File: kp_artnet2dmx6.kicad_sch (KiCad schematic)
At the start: 0 parts

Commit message: add stm32
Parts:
- added C1, C10, C3, C4, C5, C6, C7, C8: 100n, symbol Device:C_Small
- added C2: 10u, symbol Device:C_Small
- added C9: 1u, symbol Device:C_Small
- added FB1, FB2, FB3: 600@100MHz, symbol Device:FerriteBead_Small
- added R1: R_Small, symbol Device:R_Small
- added SW1: SW_SPDT, symbol Switch:SW_SPDT
- added U1: STM32F407VETx, Package_QFP:LQFP-100_14x14mm_P0.5mm, symbol MCU_ST_STM32F4:STM32F407VETx
- added Y1: 16MHz, symbol Device:Crystal_GND24_Small
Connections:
- new net: Y1.2 (G), Y1.4 (G)
- new net: R1.2, SW1.2 (B)
- new net +3.3V: C2.1, C3.1, C4.1, C5.1, C6.1, C7.1, C8.1, FB1.2, SW1.3 (C), U1.100 (VDD), U1.11 (VDD), U1.19 (VDD), U1.28 (VDD), U1.50 (VDD), U1.6 (VBAT), U1.75 (VDD)
- new net +3.3VA: C10.1, C9.1, FB1.1, FB3.2, U1.22 (VDDA)
- new net +3.3VREF: C1.1, FB3.1, U1.21 (VREF+)
- new net GND: C2.2, C3.2, C4.2, C5.2, C6.2, C7.2, C8.2, FB2.2, SW1.1 (A), U1.10 (VSS), U1.27 (VSS), U1.74 (VSS), U1.99 (VSS)
- new net GNDA: C1.2, C10.2, C9.2, FB2.1, U1.20 (VSSA)
- new net STM_BOOT0: R1.1, U1.94 (BOOT0)
- new net STM_HSE_IN: U1.12 (PH0)
- new net STM_HSE_OUT: U1.13 (PH1)
- new net STM_NRST: U1.14 (NRST)
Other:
- note added: "BOOT0: LOW for normal boot HIGH for bootloader"
- note added: "TODO"
- note added: "decoupling caps + vdd/vdda connection"

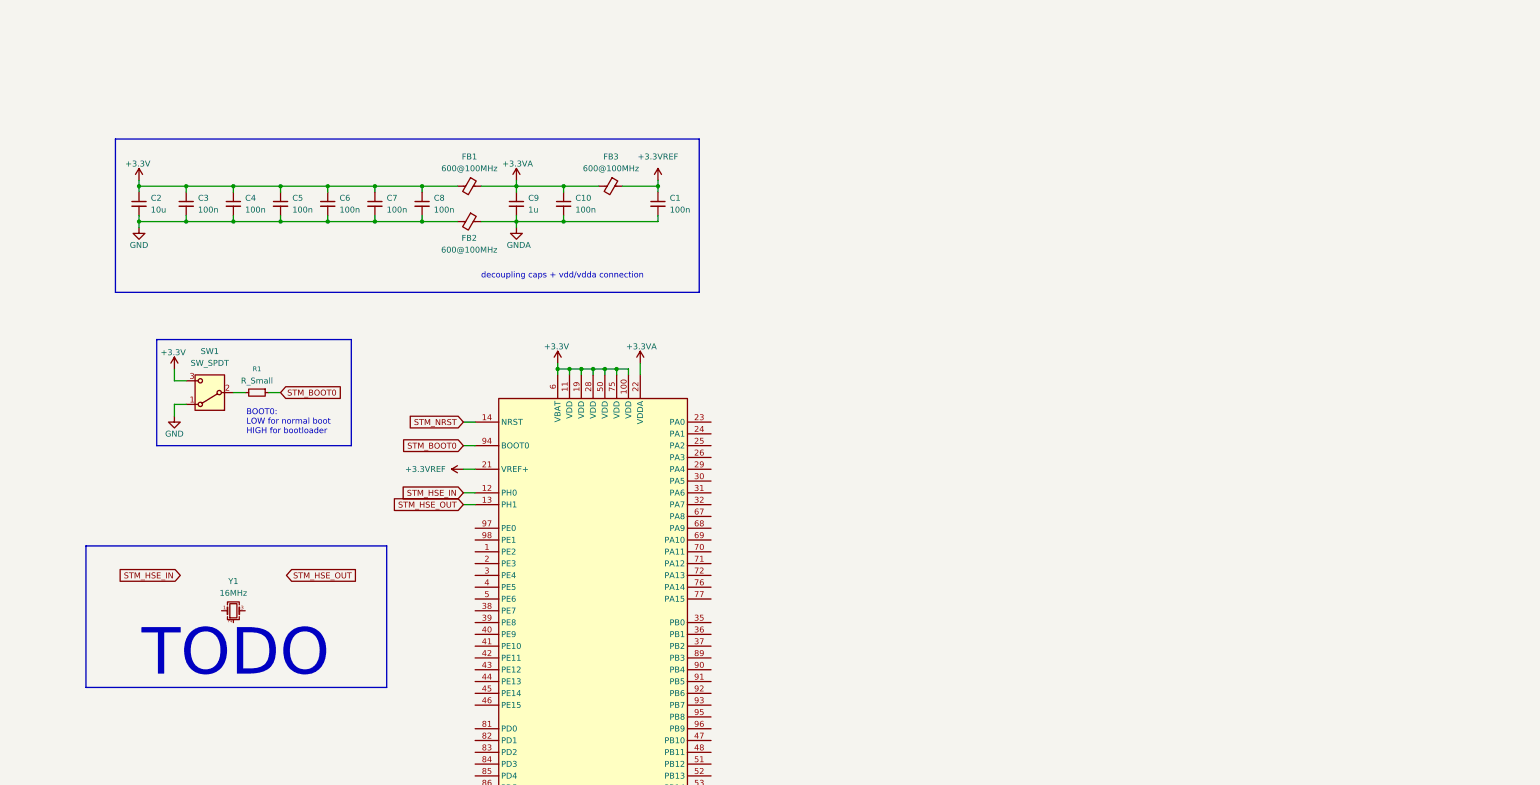
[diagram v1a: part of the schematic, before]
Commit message: sch: add phy, add oscillator
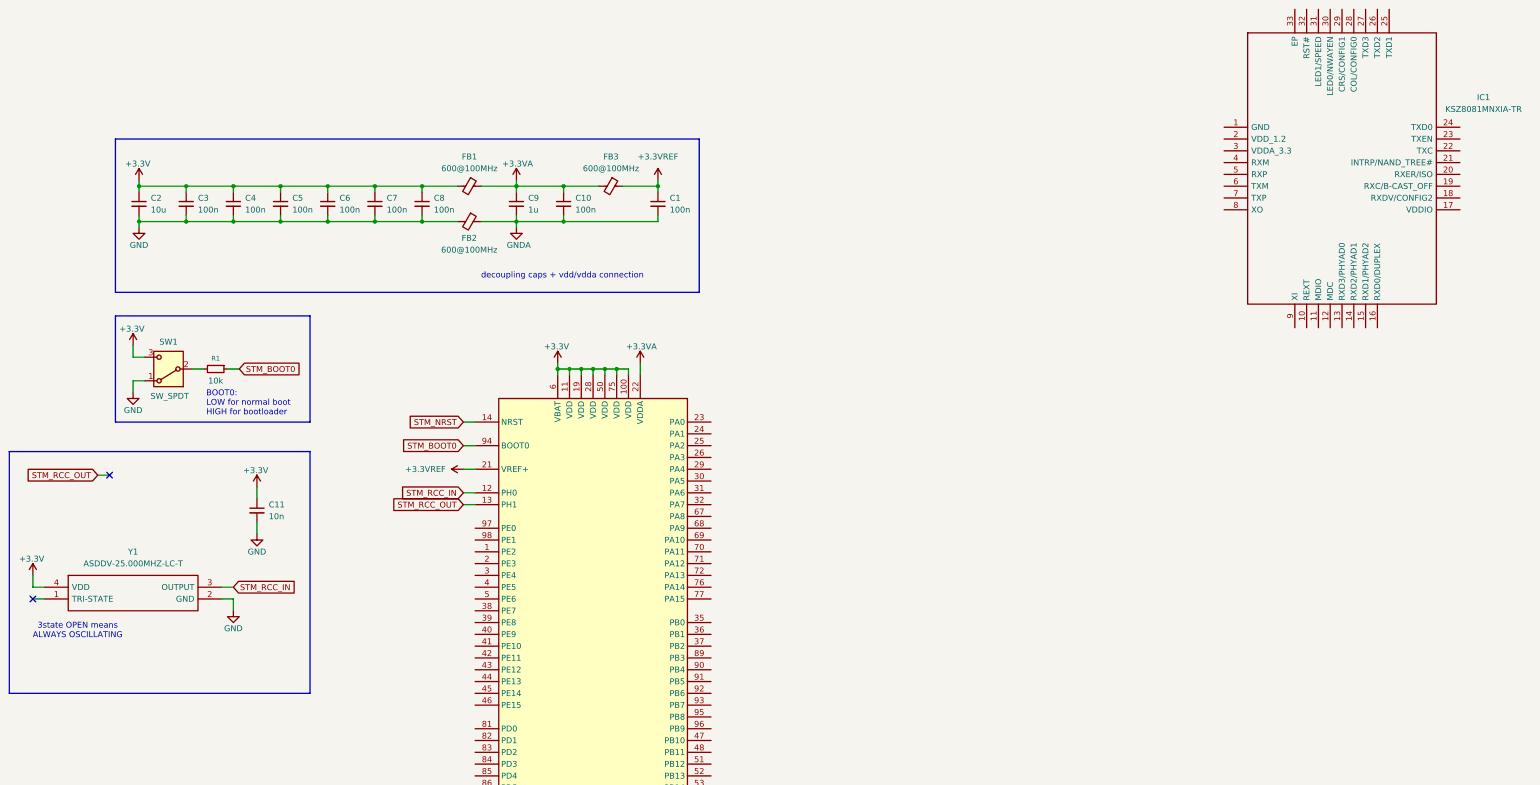
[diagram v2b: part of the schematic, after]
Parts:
- removed Y1: 16MHz, symbol Device:Crystal_GND24_Small
- added C11: 10n, symbol Device:C_Small
- added IC1: KSZ8081MNXIA-TR, QFN50P500X500X100-33N-D, symbol SamacSys:KSZ8081MNXIA-TR
- added Y1: ASDDV-25.000MHZ-LC-T, AbraconASDDV, symbol SamacSys:ASDDV-25.000MHZ-LC-T
- R1: value R_Small -> 10k
- SW1: footprint (none) -> Button_Switch_SMD:SW_SPDT_PCM12
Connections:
- net +3.3V: now also C11.1, Y1.4 (VDD)
- net GND: now also C11.2, Y1.2 (GND)
- net STM_HSE_IN renamed STM_RCC_IN
- net STM_RCC_IN: now also Y1.3 (OUTPUT)
- net STM_HSE_OUT renamed STM_RCC_OUT
- no-connect marks 0 -> 2
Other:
- note added: "3state OPEN means ALWAYS OSCILLATING"
- note removed: "TODO"
- moved on the sheet: R1, SW1

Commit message: add ksz eth controller, todo finish connecting it
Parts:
- added C12: 2.2u, symbol Device:C_Small
- added C13, C17, C19: 100n, symbol Device:C_Small
- added C16, C18: 22u, symbol Device:C_Small
- added FB5: 600@100MHz, symbol Device:FerriteBead_Small
- added J1: RJ45_Amphenol_RJMG1BD3B8K1ANR, Connector_RJ:RJ45_Amphenol_RJMG1BD3B8K1ANR, symbol Connector:RJ45_Amphenol_RJMG1BD3B8K1ANR
- added R2: 1k, symbol Device:R_Small
- added R3: 4.49k, symbol Device:R_Small
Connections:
- net +3.3V: now also IC1.17 (VDDIO), C16.1, C17.1, FB5.2, R2.2
- net GND: now also IC1.1 (GND), C12.2, C13.2, C16.2, C17.2, C18.2, C19.2, R3.1
- net at IC1.10 (REXT): now also R3.2
- net STM_ETH_MDIO: now reaches IC1.11 (MDIO)
- net STM_ETH_MDIO: now also U1.25 (PA2), R2.1
- net STM_ETH_MDC: now reaches IC1.12 (MDC)
- net STM_ETH_MDC: now also U1.16 (PC1)
- net KSZ_VDD_1.2: now reaches IC1.2 (VDD_1.2)
- net KSZ_VDDA_3.3: now reaches IC1.3 (VDDA_3.3)
- net KSZ_VDDA_3.3: now also C18.1, C19.1, FB5.1
- net KSZ_RXM: now reaches IC1.4 (RXM)
- net KSZ_RXM: now also J1.R6 (RD-)
- net KSZ_RXP: now reaches IC1.5 (RXP)
- net KSZ_RXP: now also J1.R3 (RD+)
- net KSZ_TXM: now reaches IC1.6 (TXM)
- net KSZ_TXM: now also J1.R2 (TD-)
- net KSZ_TXP: now reaches IC1.7 (TXP)
- net KSZ_TXP: now also J1.R1 (TD+)
- net STM_RCC_MCO_1: now reaches IC1.9 (XI)
- net STM_RCC_MCO_1: now also U1.67 (PA8)
- net STM_ETH_TXD3: now reaches U1.1 (PE2)
- net STM_ETH_TXD2: now reaches U1.17 (PC2)
- net STM_ETH_CRS: now reaches U1.23 (PA0)
- net STM_ETH_RX_CLK: now reaches U1.24 (PA1)
- net STM_ETH_COL: now reaches U1.26 (PA3)
- net STM_ETH_RX_DV: now reaches U1.32 (PA7)
- net STM_ETH_RXD0: now reaches U1.33 (PC4)
- net STM_ETH_RXD1: now reaches U1.34 (PC5)
- net STM_ETH_RXD2: now reaches U1.35 (PB0)
- net STM_ETH_RXD3: now reaches U1.36 (PB1)
- net STM_ETH_TX_EN: now reaches U1.48 (PB11)
- net STM_ETH_TXD0: now reaches U1.51 (PB12)
- net STM_ETH_TXD1: now reaches U1.52 (PB13)
- new net KSZ_VDD_1.2V: C12.1, C13.1
- no-connect marks 2 -> 3
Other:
- note added: "KSZ8081MNX/RNB POWER PIN DESCRIPTIONS Power Pin Pin Number Description VDD_1.2 2 Decouple with 2.2 μF and 0.1 μF capacitors to ground. VDDA_3.3 3 Connect to board's 3.3V supply through a ferrite bead. Decouple with 22 μF and 0.1 μF capacitors to ground. VDDIO 17 Connect to board's 3.3V supply for 3.3V VDDIO. Decouple with 22 μF and 0.1 μF capacitors to ground."
- moved on the sheet: IC1

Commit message: connect ksz
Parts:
- added C14: 10uF, symbol Device:C_Polarized_Small
- added C15, C20: 100n, symbol Device:C_Small
- added D1: 1N4148, Diode_THT:D_DO-35_SOD27_P7.62mm_Horizontal, symbol Diode:1N4148
- added R10, R12, R13, R15, R16, R4, R9: 1k, symbol Device:R_Small
- added R11, R14, R17, R18, R7, R8: 4.7k, symbol Device:R_Small
- added R5, R6: 220, symbol Device:R_Small
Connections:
- net +3.3V: now also D1.1 (K), R11.1, R14.2, R17.1, R18.1, R5.1, R6.1, R7.1, R8.1
- net GND: now also IC1.33 (EP), J1.R8, J1.SH, C14.2, C15.2, C20.1, R10.1, R12.2, R13.2, R15.1, R16.1, R4.2, R9.1
- net STM_ETH_COL: now also IC1.28 (COL/CONFIG0), R16.2
- net STM_ETH_CRS: now also IC1.29 (CRS/CONFIG1), R15.2
- net STM_ETH_RXD0: now also IC1.16 (RXD0/DUPLEX), R11.2
- net STM_ETH_RXD1: now also IC1.15 (RXD1/PHYAD2), R10.2
- net STM_ETH_RXD2: now also IC1.14 (RXD2/PHYAD1), R9.2
- net STM_ETH_RXD3: now also IC1.13 (RXD3/PHYAD0), R8.2
- net STM_ETH_RX_CLK: now also IC1.19 (RXC/B-CAST_OFF), R12.1
- net STM_ETH_RX_DV: now also IC1.18 (RXDV/CONFIG2), R4.1
- net STM_ETH_TXD0: now also IC1.24 (TXD0)
- net STM_ETH_TXD1: now also IC1.25 (TXD1)
- net STM_ETH_TXD2: now also IC1.26 (TXD2)
- net STM_ETH_TXD3: now also IC1.27 (TXD3)
- net STM_ETH_TX_EN: now also IC1.23 (TXEN)
- net at J1.L1: now also R5.2
- net KSZ_LED0: now reaches J1.L2
- net KSZ_LED0: now also IC1.30 (LED0/NWAYEN), R17.2
- net KSZ_LED1: now reaches J1.L3
- net KSZ_LED1: now also IC1.31 (LED1/SPEED), R18.2
- net at J1.L4: now also R6.2
- net at J1.R4 (TCT): now also C15.1
- net at J1.R5 (RCT): now also C20.2
- net STM_ETH_RXERR_GPIO: now reaches IC1.20 (RXER/ISO)
- net STM_ETH_RXERR_GPIO: now also U1.40 (PE9), R13.1
- net STM_ETH_INT_GPIO: now reaches IC1.21 (INTRP/NAND_TREE#)
- net STM_ETH_INT_GPIO: now also U1.39 (PE8), R14.1
- net STM_ETH_TX_CLK: now reaches IC1.22 (TXC)
- net STM_ETH_TX_CLK: now also U1.18 (PC3)
- net KSZ_RST: now reaches IC1.32 (RST#)
- net KSZ_RST: now also U1.38 (PE7), C14.1, D1.2 (A), R7.2
- net STM_RCC_MCO_2: now reaches U1.66 (PC9)
- net STM_RCC_MCO_2: now also IC1.9 (XI)
- net KSZ_RXM renamed KSZ_RX-
- net KSZ_RXP renamed KSZ_RX+
- net KSZ_TXM renamed KSZ_TX-
- net KSZ_TXP renamed KSZ_TX+
- net STM_RCC_MCO_1: no longer names the net of U1.67 (PA8)
- net STM_RCC_MCO_1: no longer IC1.9 (XI)
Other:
- note added: "GNDS is the chassis ground. Should it be better separeted from GND ?"
- note added: "Strap-In Options - KSZ8081MNX The strap-in pins are latched at the de-assertion of reset. In some systems, the MAC RMII receive input pins may drive high/low during power-up or reset, and consequently cause the PHY strap-in pins on the RMII signals to be latched to unintended high/low states. In this case, external pull-ups (4.7 kΩ) or pull-downs (1.0 kΩ) should be added on these PHY strap-in pin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"
- moved on the sheet: C1, C10, C11, C12, C13, C16, C17, C18, C19, C2, C3, C4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

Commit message: add eeprom
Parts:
- added IC2: M95640-RMN6P, SOIC127P600X175-8N, symbol SamacSys:M95640-RMN6P
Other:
- note added: "here GNDS is the chassis ground. Should it be better separeted from GND ?"
- note removed: "GNDS is the chassis ground. Should it be better separeted from GND ?"
- moved on the sheet: C1, C10, C11, C12, C13, C14, C15, C16, C17, C18, C19, C2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

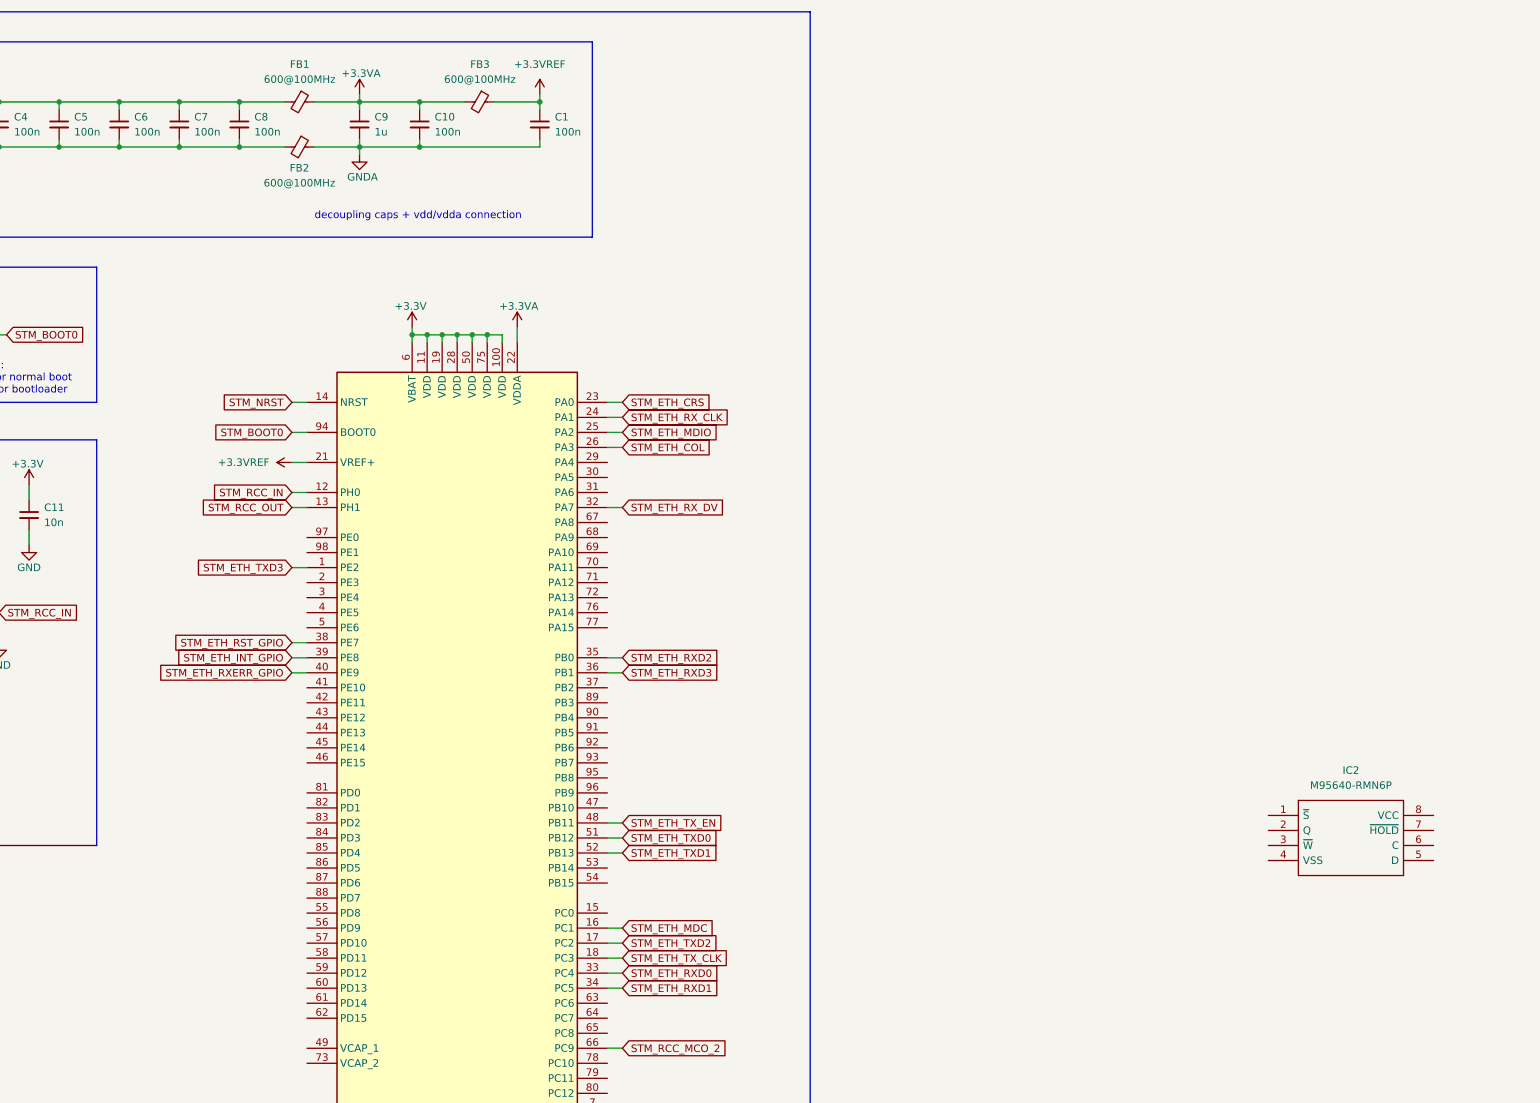
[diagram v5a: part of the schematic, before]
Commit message: connect eeprom
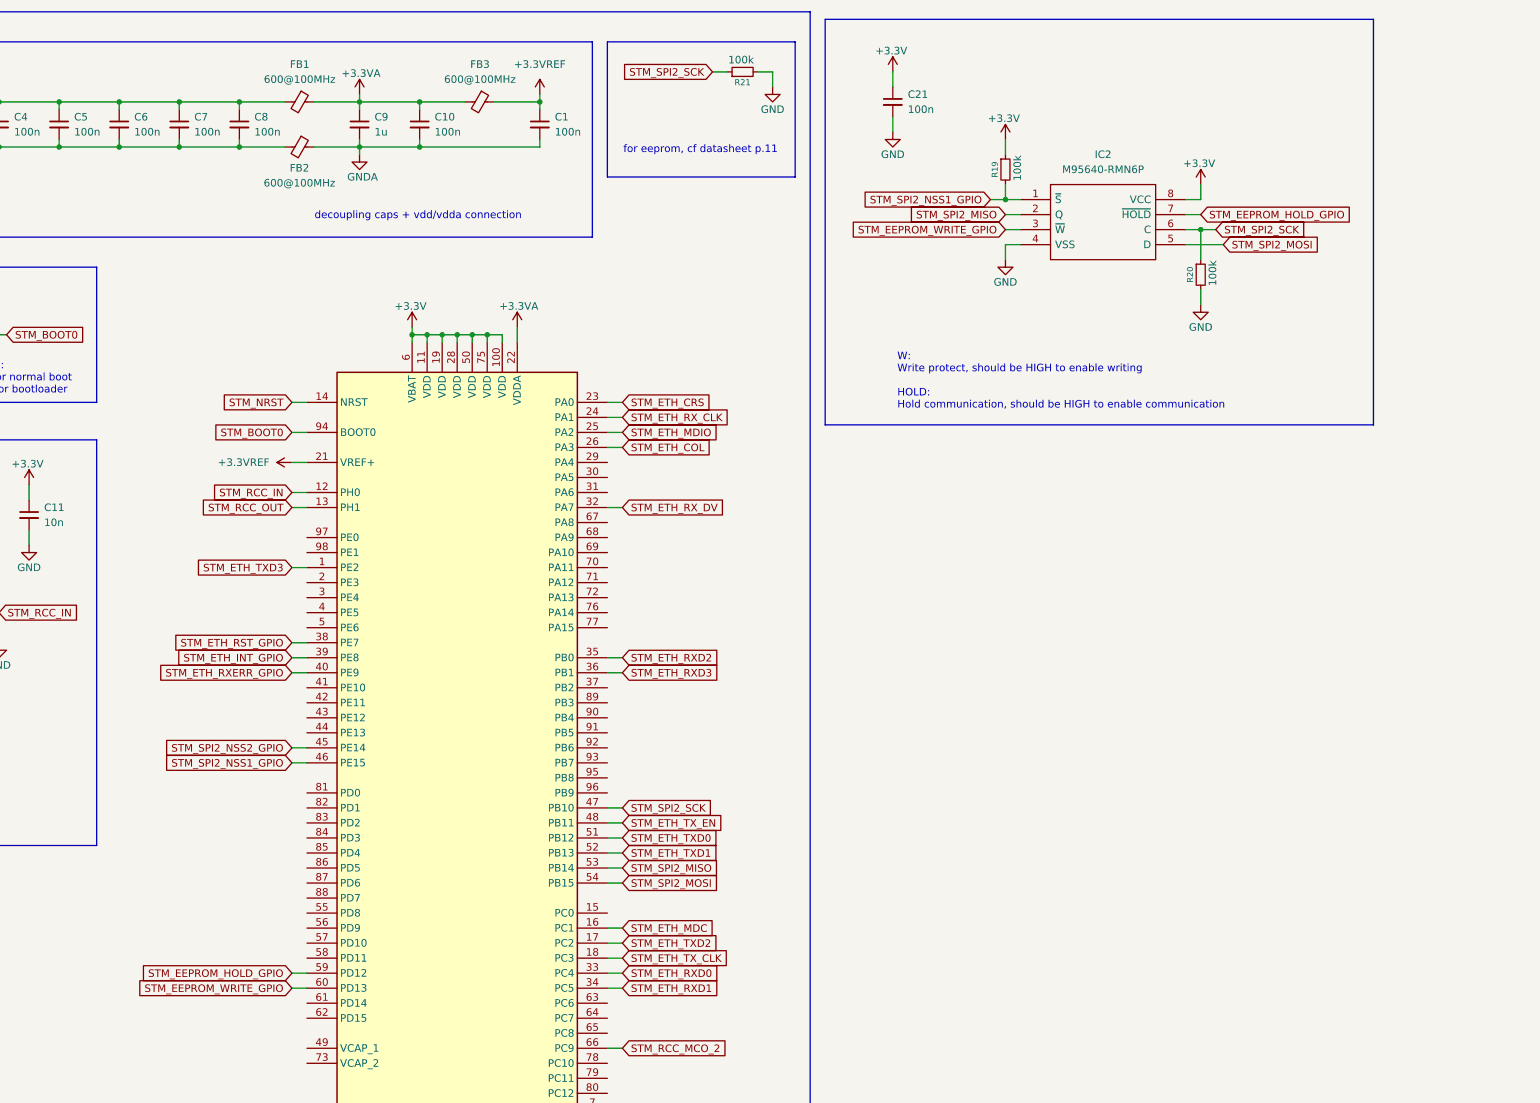
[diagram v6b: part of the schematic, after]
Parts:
- added C21: 100n, symbol Device:C_Small
- added R19, R20, R21: 100k, symbol Device:R_Small
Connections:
- net +3.3V: now also IC2.8 (VCC), C21.1, R19.1
- net GND: now also IC2.4 (VSS), C21.2, R20.2, R21.2
- net STM_SPI2_NSS1_GPIO: now reaches IC2.1 (~{S})
- net STM_SPI2_NSS1_GPIO: now also U1.46 (PE15), R19.2
- net STM_SPI2_MISO: now reaches IC2.2 (Q)
- net STM_SPI2_MISO: now also U1.53 (PB14)
- net STM_EEPROM_WRITE_GPIO: now reaches IC2.3 (~{W})
- net STM_EEPROM_WRITE_GPIO: now also U1.60 (PD13)
- net STM_SPI2_MOSI: now reaches IC2.5 (D)
- net STM_SPI2_MOSI: now also U1.54 (PB15)
- net STM_SPI2_SCK: now reaches IC2.6 (C)
- net STM_SPI2_SCK: now also U1.47 (PB10), R20.1, R21.1
- net STM_EEPROM_HOLD_GPIO: now reaches IC2.7 (~{HOLD})
- net STM_EEPROM_HOLD_GPIO: now also U1.59 (PD12)
- net STM_SPI2_NSS2_GPIO: now reaches U1.45 (PE14)
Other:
- note added: "W: Write protect, should be HIGH to enable writing HOLD: Hold communication, should be HIGH to enable communication"
- note added: "for eeprom, cf datasheet p.11"
- moved on the sheet: IC2
